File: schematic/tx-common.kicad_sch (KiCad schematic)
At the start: 26 parts, among them Q12 2N3904, Q16 2N7000, Q17 2N3906, U17 ADE-1L

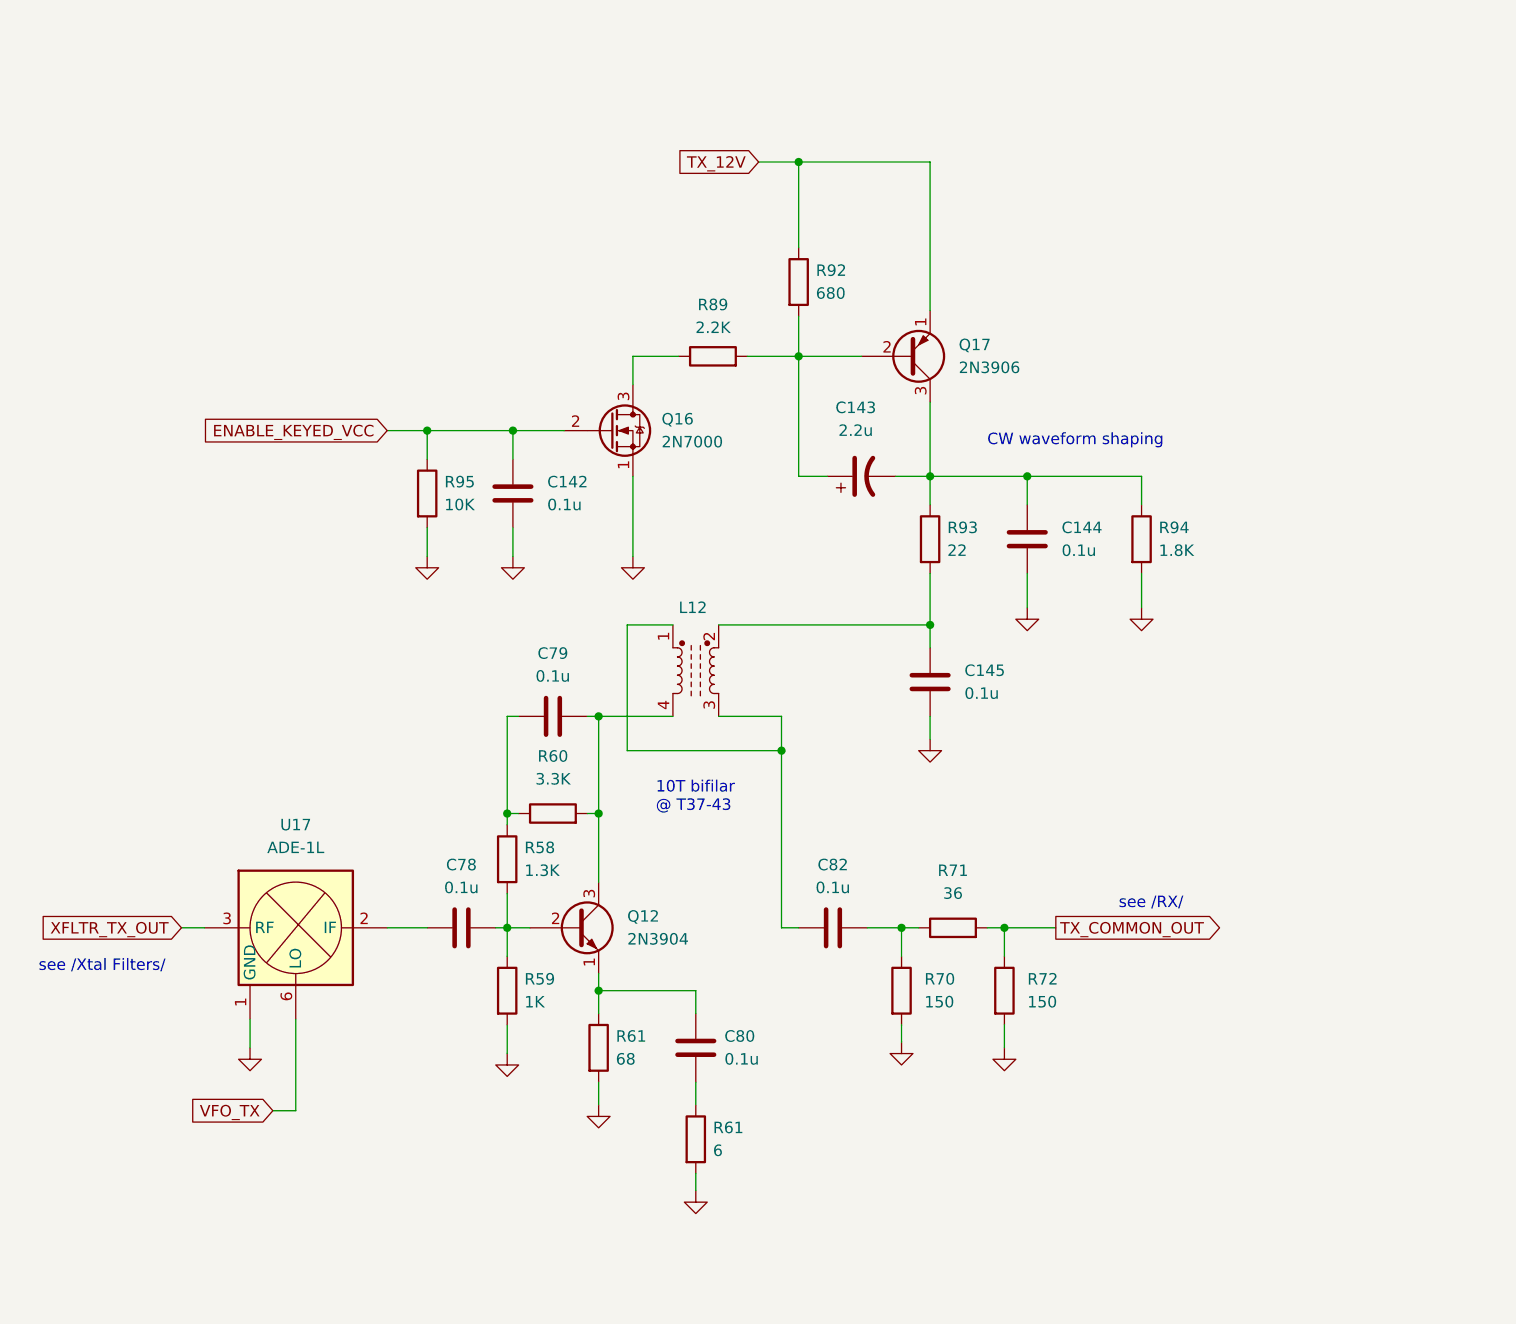
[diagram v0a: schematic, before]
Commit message: Schematic: minor changes
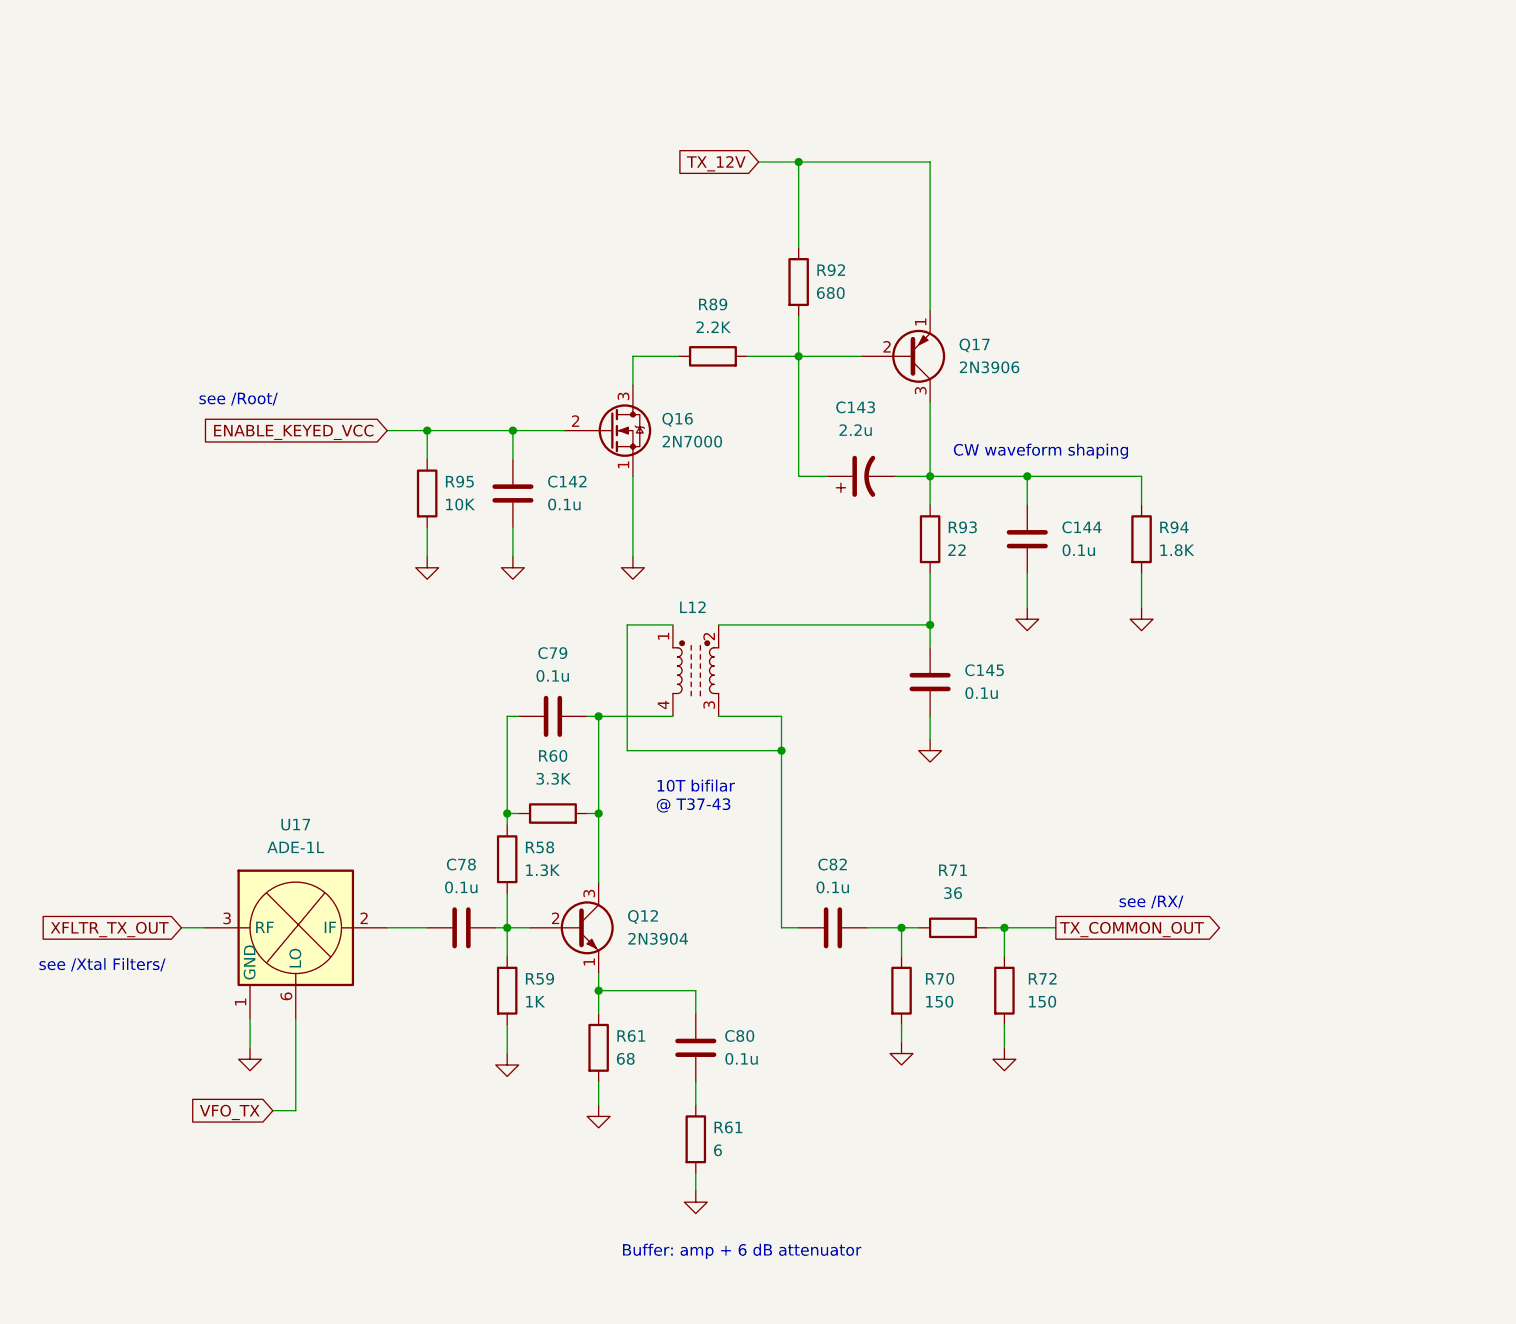
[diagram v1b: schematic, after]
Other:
- note added: "Buffer: amp + 6 dB attenuator"
- note added: "see /Root/"
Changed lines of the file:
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@@
     (stroke (width 0) (type default))
+  )
+  (text "see /Root/" (at 84.455 69.85 0)
+    (effects (font (size 1.27 1.27)) (justify left bottom))
   )
   (text "see /Xtal Filters/" (at 66.675 132.715 0)
@@
     (effects (font (size 1.27 1.27)) (justify left bottom))
   )
+  (text "Buffer: amp + 6 dB attenuator" (at 131.445 164.465 0)
+    (effects (font (size 1.27 1.27)) (justify left bottom))
+  )
   (text "10T bifilar\n@ T37-43" (at 135.255 114.935 0)
     (effects (font (size 1.27 1.27)) (justify left bottom))
   )
-  (text "CW waveform shaping\n" (at 172.085 74.295 0)
+  (text "CW waveform shaping\n" (at 168.275 75.565 0)
     (effects (font (size 1.27 1.27)) (justify left bottom))
   )

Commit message: Update schematic + minor changes
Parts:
- added D22: 1N4148, Diode_THT:D_DO-35_SOD27_P7.62mm_Horizontal, symbol Diode:1N4148
- added R60 (x2), R83: 30, symbol Device:R
- added RL3: HFD4/12, Relay_THT:Relay_DPDT_Omron_G2RL, symbol Relay:G2RL-2-ASI-DC5
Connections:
- net GND: now also D22.2 (A), R83.2, RL3.5, RL3.6, RL3.7, RL3.8
- net at C78.1: now also RL3.3; no longer U17.2 (IF)
- new net: R60.2, RL3.2
- new net: RL3.4, U17.2 (IF)
- new net: R60.1, R60.2, R83.1
- new net CLK_CW: R60.1
- new net SSB_TX_12V: D22.1 (K), RL3.1
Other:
- note added: "12 dB attenuator"
- note added: "CW"
- note added: "SSB"
- note added: "see /VFO/"
- moved on the sheet: C142, C143, C144, C145, C78, C79, C80, C82, L12, Q12, Q16, Q17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

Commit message: Update schematic
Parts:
- removed R60 (x2), R83: 30, symbol Device:R
- added R59 (x2), R60: 82, symbol Device:R
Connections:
- net CLK_CW: now also R59.1, R60.1
- net GND: now also R59.2, R59.2
- net at RL3.2: now also R59.1, R60.2

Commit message: Schematic: minor changes
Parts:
- removed Q12: 2N3904, Package_TO_SOT_THT:TO-92_Inline, symbol Transistor_BJT:2N3904
- added Q19: KT3142/2N2369, symbol Device:Q_NPN_BEC
- U17: value ADE-1L -> ADE-6
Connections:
- net at C80.2, R61.1: now also Q19.2 (E)
- net at C78.2, R58.2, R59.1: now also Q19.1 (B)
- net at C79.2, L12.4, R60.2: now also Q19.3 (C)
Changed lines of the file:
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@@
-    )
-  )
-  (symbol (lib_id "Transistor_BJT:2N3904") (at 154.305 113.03 0) (unit 1)
-    (in_bom yes) (on_board yes) (dnp no) (fields_autoplaced)
-    (property "Reference" "Q12" (at 160.02 111.76 0)
-      (effects (font (size 1.27 1.27)) (justify left))
-    )
-    (property "Value" "2N3904" (at 160.02 114.3 0)
-      (effects (font (size 1.27 1.27)) (justify left))
-    )
-    (property "Footprint" "Package_TO_SOT_THT:TO-92_Inline" (at 159.385 114.935 0)
-      (effects (font (size 1.27 1.27) italic) (justify left) hide)
-    )
-    (property "Datasheet" "https://www.onsemi.com/pub/Collateral/2N3903-D.PDF" (at 154.305 113.03 0)
-      (effects (font (size 1.27 1.27)) (justify left) hide)
-    )
-    (pin "1")
-    (pin "2")
-    (pin "3")
-    (instances
-      (project "hbr-mk2"
-        (path "/700c9878-4ed7-49d5-a273-77cf9d92989d/0b45878c-17b8-4be8-9884-0f2bddd34788"
-          (reference "Q12") (unit 1)
-        )
-        (path "/700c9878-4ed7-49d5-a273-77cf9d92989d/510b993f-d652-41da-8b0c-b7668be8d7c3"
-          (reference "Q18") (unit 1)
-        )
-        (path "/700c9878-4ed7-49d5-a273-77cf9d92989d/86d9728c-6234-48b6-9832-cb64f716a194"
-          (reference "Q18") (unit 1)
-        )
-      )
     )
   )
@@
       (effects (font (size 1.27 1.27)))
     )
-    (property "Value" "ADE-1L" (at 95.885 139.065 0)
+    (property "Value" "ADE-6" (at 95.885 139.065 0)
       (effects (font (size 1.27 1.27)))
     )
@@
         )
       )
+    )
+  )
+  (symbol (lib_id "Device:Q_NPN_BEC") (at 154.305 113.03 0) (unit 1)
+    (in_bom yes) (on_board yes) (dnp no) (fields_autoplaced)
+    (property "Reference" "Q19" (at 160.02 111.76 0)
+      (effects (font (size 1.27 1.27)) (justify left))
+    )
+    (property "Value" "KT3142/2N2369" (at 160.02 114.3 0)
+      (effects (font (size 1.27 1.27)) (justify left))
+    )
+    (property "Footprint" "" (at 159.385 110.49 0)
+      (effects (font (size 1.27 1.27)) hide)
+    )
+    (property "Datasheet" "~" (at 154.305 113.03 0)
+      (effects (font (size 1.27 1.27)) hide)
+    )
+    (pin "1")
+    (pin "2")
+    (pin "3")
+    (instances
+      (project "hbr-mk2"
+        (path "/700c9878-4ed7-49d5-a273-77cf9d92989d/86d9728c-6234-48b6-9832-cb64f716a194"
+          (reference "Q19") (unit 1)
+        )
+      )

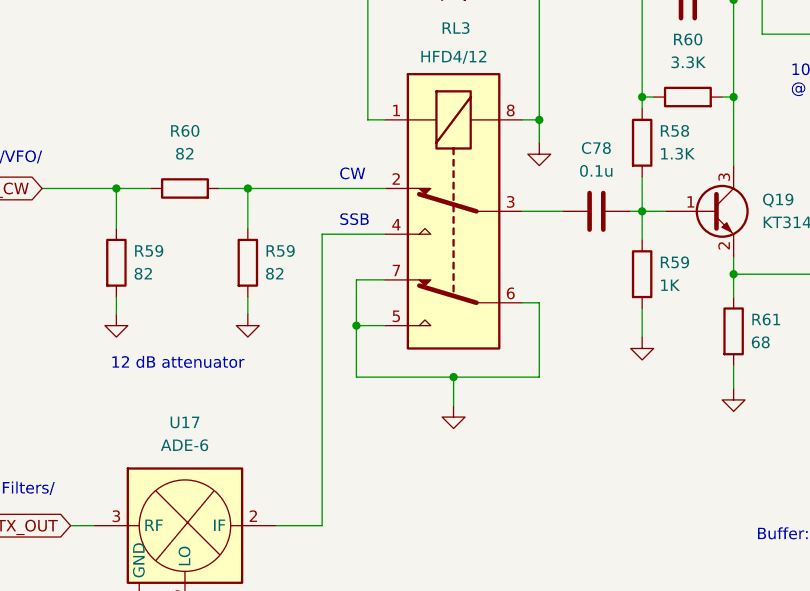
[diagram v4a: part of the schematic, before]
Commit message: Connect relay contact groups in parallel where appropriate
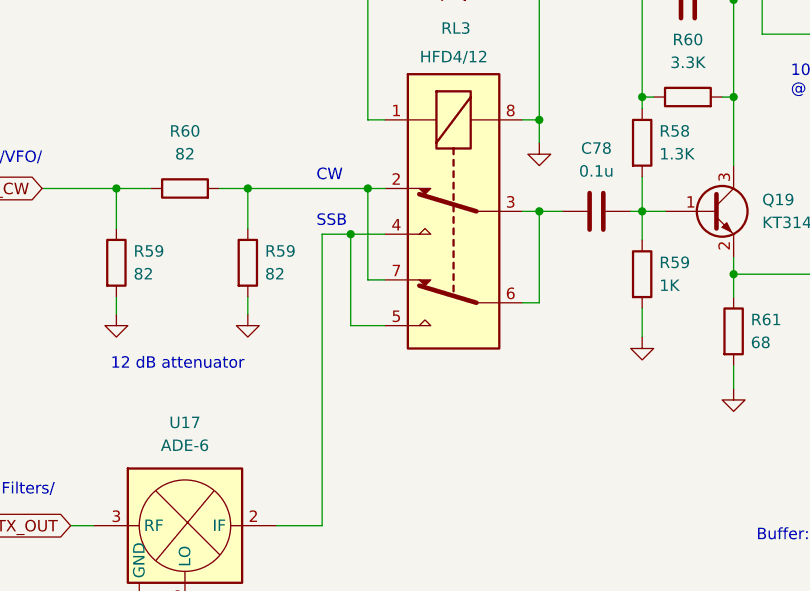
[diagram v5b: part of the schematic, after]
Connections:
- net GND: no longer RL3.5, RL3.6, RL3.7
- net at C78.1, RL3.3: now also RL3.6
- net at R59.1, R60.2, RL3.2: now also RL3.7
- net at RL3.4, U17.2 (IF): now also RL3.5
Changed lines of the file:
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@@
 (kicad_sch (version 20230121) (generator eeschema)
   (paper "A4")
-  (junction (at 114.935 125.73) (diameter 0) (color 0 0 0 0)
-  )
   (junction (at 193.675 62.865) (diameter 0) (color 0 0 0 0)
   )
   (junction (at 146.685 113.03) (diameter 0) (color 0 0 0 0)
   )
+  (junction (at 114.3 115.57) (diameter 0) (color 0 0 0 0)
+  )
   (junction (at 179.07 27.94) (diameter 0) (color 0 0 0 0)
   )
   (junction (at 204.47 62.865) (diameter 0) (color 0 0 0 0)
   )
+  (junction (at 116.205 110.49) (diameter 0) (color 0 0 0 0)
+  )
   (junction (at 177.165 93.345) (diameter 0) (color 0 0 0 0)
   )
@@
   (junction (at 137.795 57.785) (diameter 0) (color 0 0 0 0)
   )
-  (junction (at 125.73 131.445) (diameter 0) (color 0 0 0 0)
-  )
   (junction (at 135.255 102.87) (diameter 0) (color 0 0 0 0)
   )
@@
   (junction (at 193.675 79.375) (diameter 0) (color 0 0 0 0)
   )
+  (junction (at 135.255 113.03) (diameter 0) (color 0 0 0 0)
+  )
   (junction (at 116.205 88.265) (diameter 0) (color 0 0 0 0)
   )
@@
     (stroke (width 0) (type default))
   )
+  (wire (pts (xy 135.255 113.03) (xy 135.255 123.19))
+    (stroke (width 0) (type default))
+  )
   (wire (pts (xy 135.255 123.19) (xy 133.35 123.19))
     (stroke (width 0) (type default))
@@
     (stroke (width 0) (type default))
   )
-  (wire (pts (xy 135.255 131.445) (xy 135.255 123.19))
-    (stroke (width 0) (type default))
-  )
   (wire (pts (xy 160.02 93.345) (xy 177.165 93.345))
     (stroke (width 0) (type default))
@@
     (stroke (width 0) (type default))
   )
-  (wire (pts (xy 125.73 134.62) (xy 125.73 131.445))
-    (stroke (width 0) (type default))
-  )
   (wire (pts (xy 133.35 57.785) (xy 137.795 57.785))
     (stroke (width 0) (type default))
   )
-  (wire (pts (xy 133.35 113.03) (xy 137.795 113.03))
+  (wire (pts (xy 133.35 113.03) (xy 135.255 113.03))
     (stroke (width 0) (type default))
   )
@@
     (stroke (width 0) (type default))
   )
-  (wire (pts (xy 125.73 131.445) (xy 114.935 131.445))
-    (stroke (width 0) (type default))
-  )
   (wire (pts (xy 201.93 123.825) (xy 201.93 126.365))
     (stroke (width 0) (type default))
@@
     (stroke (width 0) (type default))
   )
+  (wire (pts (xy 114.3 115.57) (xy 118.11 115.57))
+    (stroke (width 0) (type default))
+  )
   (wire (pts (xy 201.93 113.03) (xy 207.645 113.03))
     (stroke (width 0) (type default))
@@
     (stroke (width 0) (type default))
   )
-  (wire (pts (xy 125.73 131.445) (xy 135.255 131.445))
-    (stroke (width 0) (type default))
-  )
   (wire (pts (xy 146.685 113.03) (xy 149.225 113.03))
     (stroke (width 0) (type default))
@@
     (stroke (width 0) (type default))
   )
+  (wire (pts (xy 114.3 125.73) (xy 114.3 115.57))
+    (stroke (width 0) (type default))
+  )
   (wire (pts (xy 193.675 27.94) (xy 193.675 44.45))
     (stroke (width 0) (type default))
@@
     (stroke (width 0) (type default))
   )
+  (wire (pts (xy 116.205 120.65) (xy 116.205 110.49))
+    (stroke (width 0) (type default))
+  )
   (wire (pts (xy 93.345 168.275) (xy 95.885 168.275))
     (stroke (width 0) (type default))
   )
-  (wire (pts (xy 114.935 125.73) (xy 114.935 120.65))
-    (stroke (width 0) (type default))
-  )
   (wire (pts (xy 146.685 89.535) (xy 147.955 89.535))
     (stroke (width 0) (type default))
@@
     (stroke (width 0) (type default))
   )
+  (wire (pts (xy 116.205 110.49) (xy 118.11 110.49))
+    (stroke (width 0) (type default))
+  )
   (wire (pts (xy 177.165 89.535) (xy 177.165 93.345))
     (stroke (width 0) (type default))
@@
     (stroke (width 0) (type default))
   )
-  (wire (pts (xy 114.935 131.445) (xy 114.935 125.73))
-    (stroke (width 0) (type default))
-  )
   (wire (pts (xy 156.845 120.015) (xy 167.64 120.015))
     (stroke (width 0) (type default))
@@
     (stroke (width 0) (type default))
   )
+  (wire (pts (xy 118.11 120.65) (xy 116.205 120.65))
+    (stroke (width 0) (type default))
+  )
   (wire (pts (xy 155.575 100.33) (xy 156.845 100.33))
     (stroke (width 0) (type default))
@@
     (stroke (width 0) (type default))
   )
-  (wire (pts (xy 114.935 120.65) (xy 118.11 120.65))
-    (stroke (width 0) (type default))
-  )
   (wire (pts (xy 88.265 110.49) (xy 88.265 114.935))
     (stroke (width 0) (type default))
@@
     (stroke (width 0) (type default))
   )
-  (wire (pts (xy 114.935 125.73) (xy 118.11 125.73))
+  (wire (pts (xy 114.3 125.73) (xy 118.11 125.73))
+    (stroke (width 0) (type default))
+  )
+  (wire (pts (xy 135.255 113.03) (xy 137.795 113.03))
     (stroke (width 0) (type default))
   )
@@
     (stroke (width 0) (type default))
   )
-  (wire (pts (xy 111.125 115.57) (xy 118.11 115.57))
+  (wire (pts (xy 111.125 115.57) (xy 114.3 115.57))
     (stroke (width 0) (type default))
   )
@@
     (stroke (width 0) (type default))
   )
-  (wire (pts (xy 102.87 110.49) (xy 118.11 110.49))
+  (wire (pts (xy 102.87 110.49) (xy 116.205 110.49))
     (stroke (width 0) (type default))
   )
@@
     (effects (font (size 1.27 1.27)) (justify left bottom))
   )
-  (text "SSB" (at 113.03 114.935 0)
+  (text "SSB" (at 110.49 114.935 0)
     (effects (font (size 1.27 1.27)) (justify left bottom))
   )
@@
     (effects (font (size 1.27 1.27)) (justify left bottom))
   )
-  (text "CW" (at 113.03 109.855 0)
+  (text "CW" (at 110.49 109.855 0)
     (effects (font (size 1.27 1.27)) (justify left bottom))
   )
@@
         )
       )
-    )
-  )
-  (symbol (lib_id "power:GND") (at 125.73 134.62 0) (unit 1)
-    (in_bom yes) (on_board yes) (dnp no) (fields_autoplaced)
-    (property "Reference" "#PWR0129" (at 125.73 140.97 0)
-      (effects (font (size 1.27 1.27)) hide)
-    )
-    (property "Value" "GND" (at 125.73 139.7 0)
-      (effects (font (size 1.27 1.27)) hide)
-    )
-    (property "Footprint" "" (at 125.73 134.62 0)
-      (effects (font (size 1.27 1.27)) hide)
-    )
-    (property "Datasheet" "" (at 125.73 134.62 0)
-      (effects (font (size 1.27 1.27)) hide)
-    )
-    (pin "1")
-    (instances
-      (project "hbr-mk2"
-        (path "/700c9878-4ed7-49d5-a273-77cf9d92989d/0b45878c-17b8-4be8-9884-0f2bddd34788"
-          (reference "#PWR0129") (unit 1)
-        )
-        (path "/700c9878-4ed7-49d5-a273-77cf9d92989d/510b993f-d652-41da-8b0c-b7668be8d7c3"
-          (reference "#PWR0246") (unit 1)
-        )
-        (path "/700c9878-4ed7-49d5-a273-77cf9d92989d/86d9728c-6234-48b6-9832-cb64f716a194"
-          (reference "#PWR0255") (unit 1)
-        )
-      )

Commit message: Add PA schematic + some minor changes
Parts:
- L12: value L_Ferrite_Coupled_1423 -> FT37-43
- Q19: value KT3142/2N2369 -> KT3142A
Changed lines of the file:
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@@
       (effects (font (size 1.27 1.27)) (justify left))
     )
-    (property "Value" "L_Ferrite_Coupled_1423" (at 164.465 85.471 90)
+    (property "Value" "FT37-43" (at 164.465 85.471 90)
       (effects (font (size 1.27 1.27)) (justify left) hide)
     )
@@
       (effects (font (size 1.27 1.27)) (justify left))
     )
-    (property "Value" "KT3142/2N2369" (at 160.02 114.3 0)
+    (property "Value" "KT3142A" (at 160.02 114.3 0)
       (effects (font (size 1.27 1.27)) (justify left))
     )

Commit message: Schematic: minor fixes
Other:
- note added: "10T bifilar @ FT37-43"
- note removed: "10T bifilar @ T37-43"
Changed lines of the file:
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@@
     (effects (font (size 1.27 1.27)) (justify left bottom))
   )
-  (text "10T bifilar\n@ T37-43" (at 163.195 100.33 0)
+  (text "10T bifilar\n@ FT37-43" (at 163.195 100.33 0)
     (effects (font (size 1.27 1.27)) (justify left bottom))
   )

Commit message: Minor changes
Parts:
- renumbered C78 to C146, C79 to C147, C80 to C148, C82 to C150, L12 to L32, R61 to R100, R70 to R102, R71 to R103, R72 to R104, R60 to R82, R59 to R83, R59 to R84, R58 to R96, R59 to R97, R60 to R98, R61 to R99, RL3 to RL26
